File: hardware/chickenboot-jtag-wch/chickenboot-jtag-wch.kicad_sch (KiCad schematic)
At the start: 24 parts, among them J1 USB_C_Receptacle_USB2.0, J2 Conn_01x03, J3 JTAG, J4 Conn_01x03, Q1 LP0404N3T5G, SW2 SW_Push, U1 CH32X035F8U6, U2 HT7533-1, U3 IS25WP016D-JULE-TR, U4 USBLC6-2P6

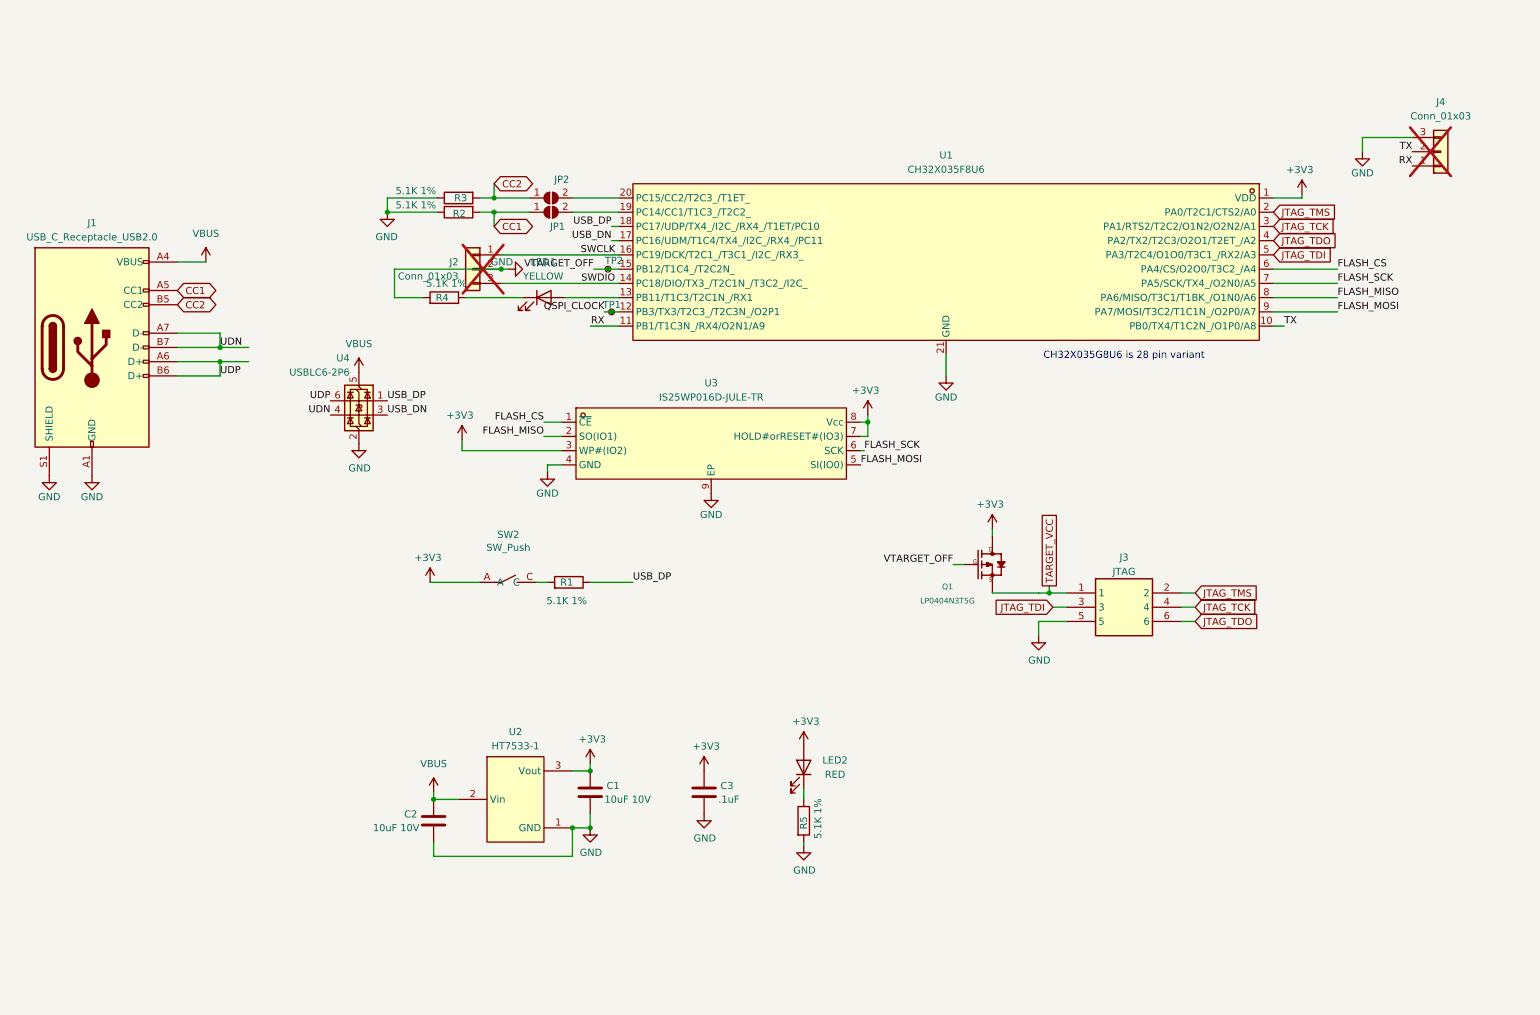
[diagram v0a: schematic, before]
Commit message: add a decouliping capacitor to flash, a pullup to PMOS power control, and clean schematics
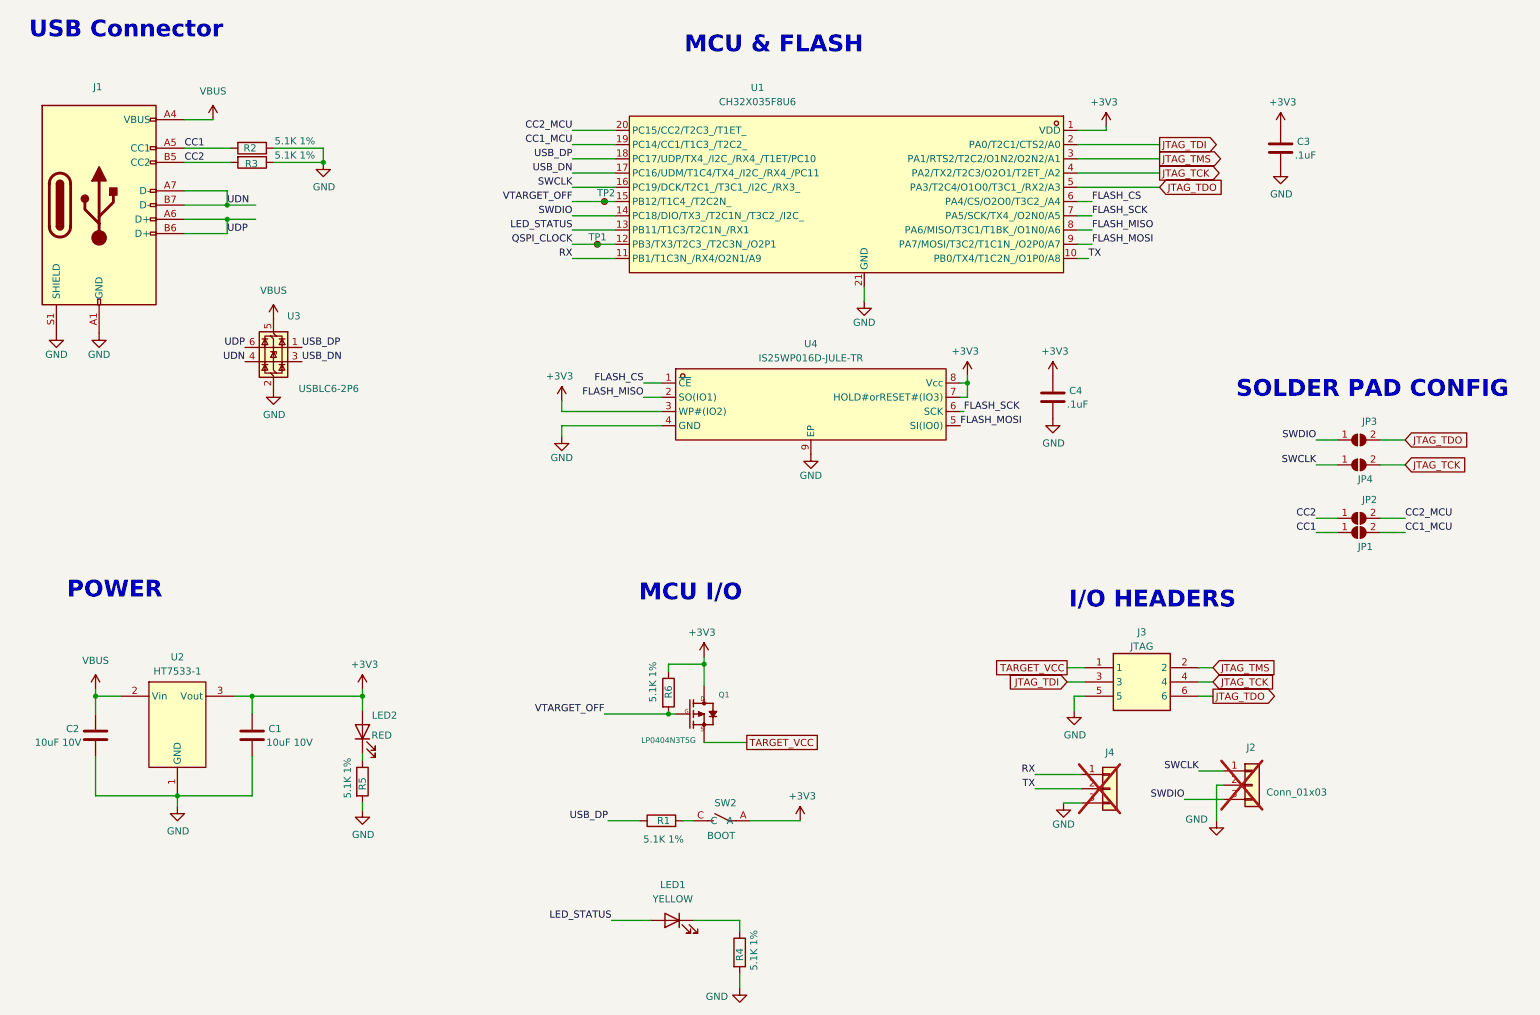
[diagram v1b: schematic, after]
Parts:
- added C4: .1uF, Capacitor_SMD:C_0402_1005Metric, symbol Device:C
- added JP3, JP4: SolderJumper_2_Open, Jumper:SolderJumper-2_P1.3mm_Open_RoundedPad1.0x1.5mm, symbol Jumper:SolderJumper_2_Open
- added R6: 5.1K 1%, Resistor_SMD:R_0402_1005Metric, symbol Device:R
- SW2: value SW_Push -> BOOT
- renumbered U4 to U3, U3 to U4
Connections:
- net +3V3: now also C4.1, R6.1
- net GND: now also C4.2
- net JTAG_TCK: now also U1.4 (PA2/TX2/T2C3/O2O1/T2ET_/A2), JP4.2 (B); no longer U1.3 (PA1/RTS2/T2C2/O1N2/O2N2/A1)
- net JTAG_TDI: now also U1.2 (PA0/T2C1/CTS2/A0); no longer U1.5 (PA3/T2C4/O1O0/T3C1_/RX2/A3)
- net JTAG_TDO: now also U1.5 (PA3/T2C4/O1O0/T3C1_/RX2/A3), JP3.2 (B); no longer U1.4 (PA2/TX2/T2C3/O2O1/T2ET_/A2)
- net JTAG_TMS: now also U1.3 (PA1/RTS2/T2C2/O1N2/O2N2/A1); no longer U1.2 (PA0/T2C1/CTS2/A0)
- net SWCLK: now also JP4.1 (A)
- net SWDIO: now also JP3.1 (A)
- net VTARGET_OFF: now also R6.2
- net CC2_MCU: now reaches JP2.2 (B), U1.20 (PC15/CC2/T2C3_/T1ET_)
- net LED_STATUS: now reaches LED1.2 (A), U1.13 (PB11/T1C3/T2C1N_/RX1)
- net CC1_MCU: now reaches JP1.2 (B), U1.19 (PC14/CC1/T1C3_/T2C2_)
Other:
- note added: "I/O HEADERS"
- note added: "MCU & FLASH"
- note added: "MCU I/O"
- note added: "POWER"
- note added: "SOLDER PAD CONFIG"
- note added: "USB Connector"
- note removed: "CH32X035G8U6 is 28 pin variant"
- company: (none) -> (C) 2026 Victor Suarez Rovere
- title: (none) -> ChickenBoot
- moved on the sheet: C3, J1, LED2, R1, R5, SW2, TP1, TP2, U1, U3, U4

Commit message: change boards shape and fixes for manufacturability
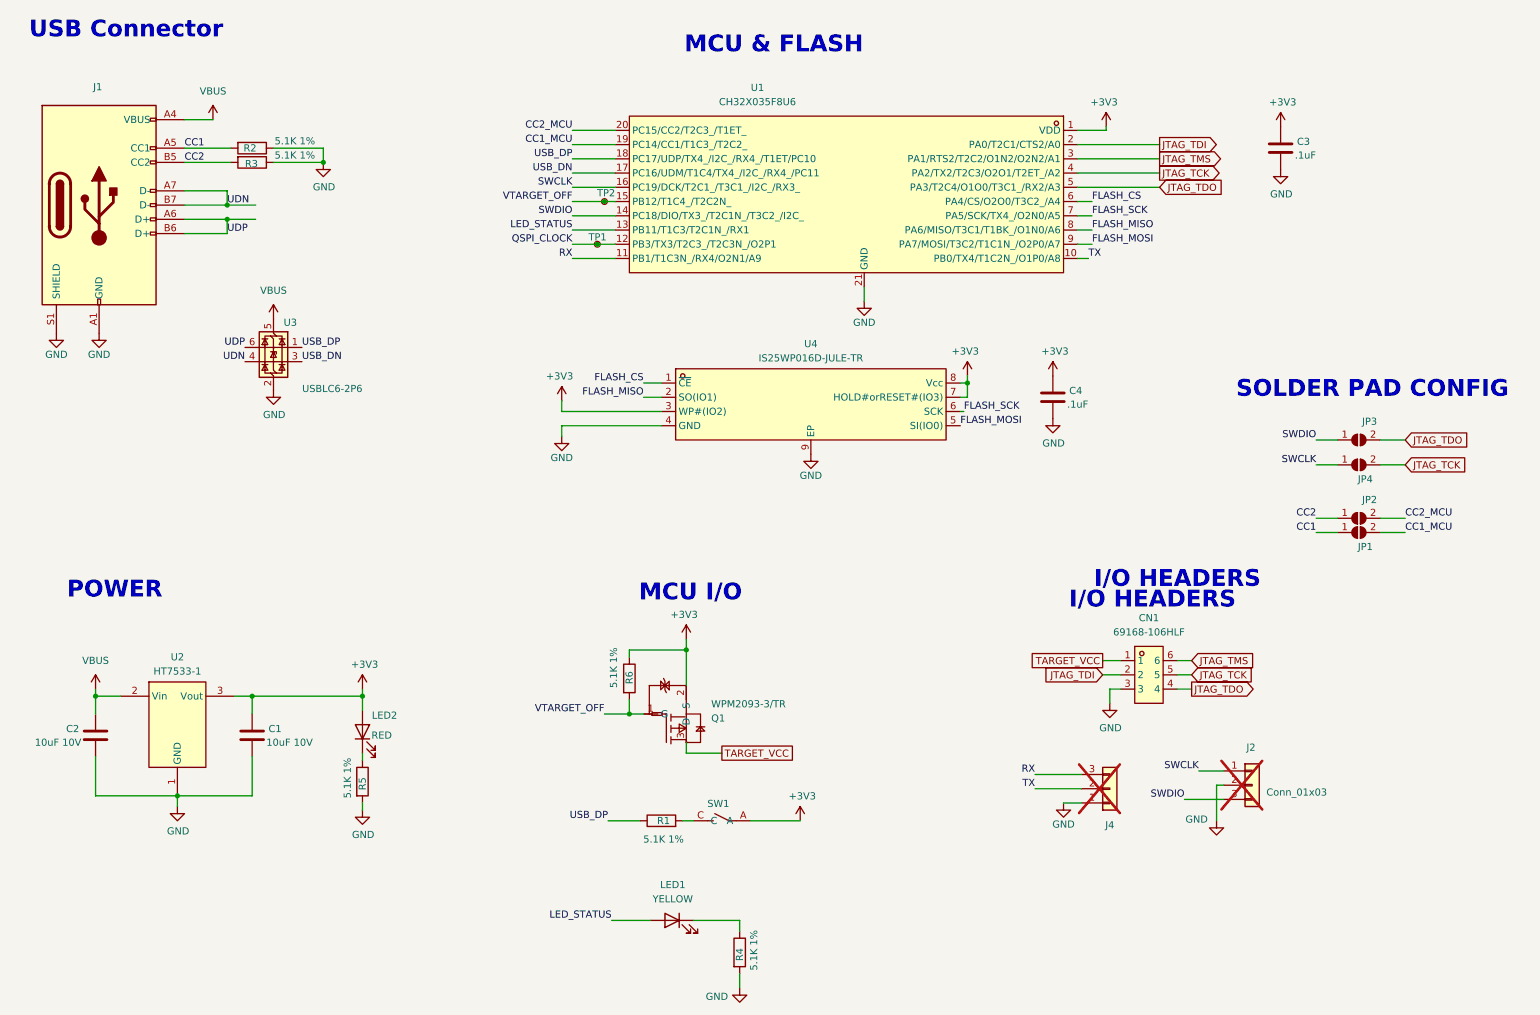
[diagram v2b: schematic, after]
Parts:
- removed J3: JTAG, Connector_IDC:IDC-Header_2x03_P2.54mm_Vertical, symbol PRT-12807:PRT-12807
- removed Q1: LP0404N3T5G, Package_TO_SOT_SMD:SOT-883, symbol Seeed_libadl:Mosfet/305031466
- removed SW2: BOOT, easyeda2kicad:SW-SMD_4P-L2.5-W1.6-LS2.9_STI-055A12AX, symbol easyeda2kicad:GT-TC194A-H0055-L1
- added CN1: 69168-106HLF, easyeda2kicad:CONN-TH_6P-P2.54_69168-X06, symbol easyeda2kicad:69168-106HLF
- added Q1: WPM2093-3/TR, easyeda2kicad:SOT-723_L1.2-W0.8-P0.80-LS1.2-BR, symbol easyeda2kicad:WPM2093-3_TR
- added SW1: SW_Push, easyeda2kicad:SW-SMD_4P-L2.5-W1.6-LS2.9_STI-055A12AX, symbol easyeda2kicad:GT-TC194A-H0055-L1
- U3: LCSC Part Number (none) -> C15999; MPN (none) -> USBLC6-2P6
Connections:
- net +3V3: now also Q1.2 (S), SW1.A
- net GND: now also J4.1 (Pin_1), CN1.3; no longer J4.3 (Pin_3)
- net JTAG_TCK: now also CN1.5
- net JTAG_TDI: now also CN1.2
- net JTAG_TDO: now also CN1.4
- net JTAG_TMS: now also CN1.6
- net RX: now also J4.3 (Pin_3); no longer J4.1 (Pin_1)
- net TARGET_VCC: now also CN1.1, Q1.3 (D)
- net VTARGET_OFF: now also Q1.1 (G)
- net at R1.2: now also SW1.C
